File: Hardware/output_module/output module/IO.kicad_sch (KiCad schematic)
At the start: 30 parts, among them J2 thonkiconn, J3 thonkiconn, J4 Conn_01x03, J4 thonkiconn, U1 MAX97220C, U2 TL074

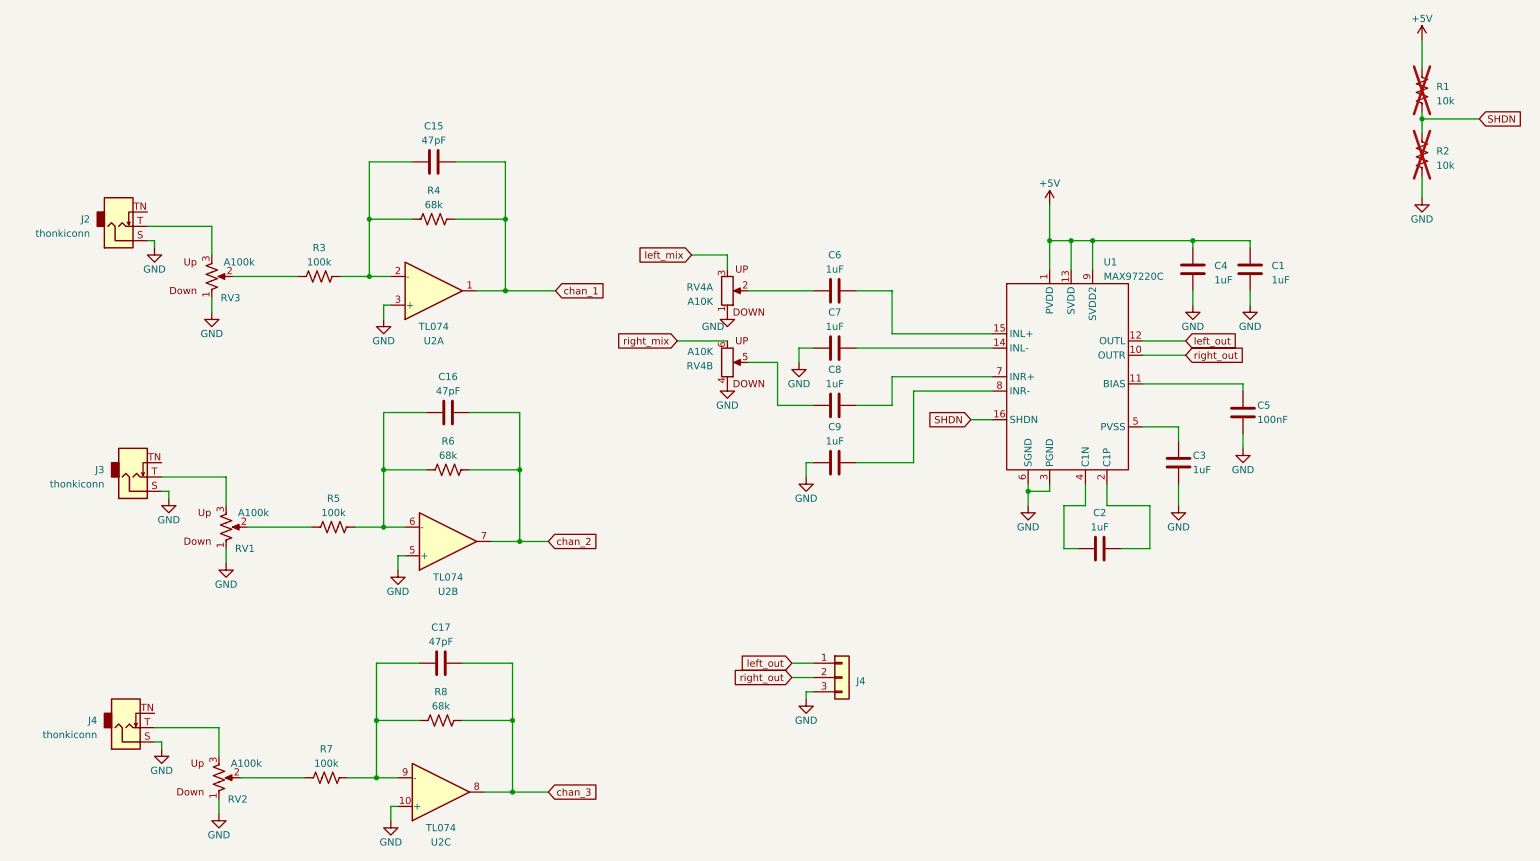
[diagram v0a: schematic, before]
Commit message: proto order
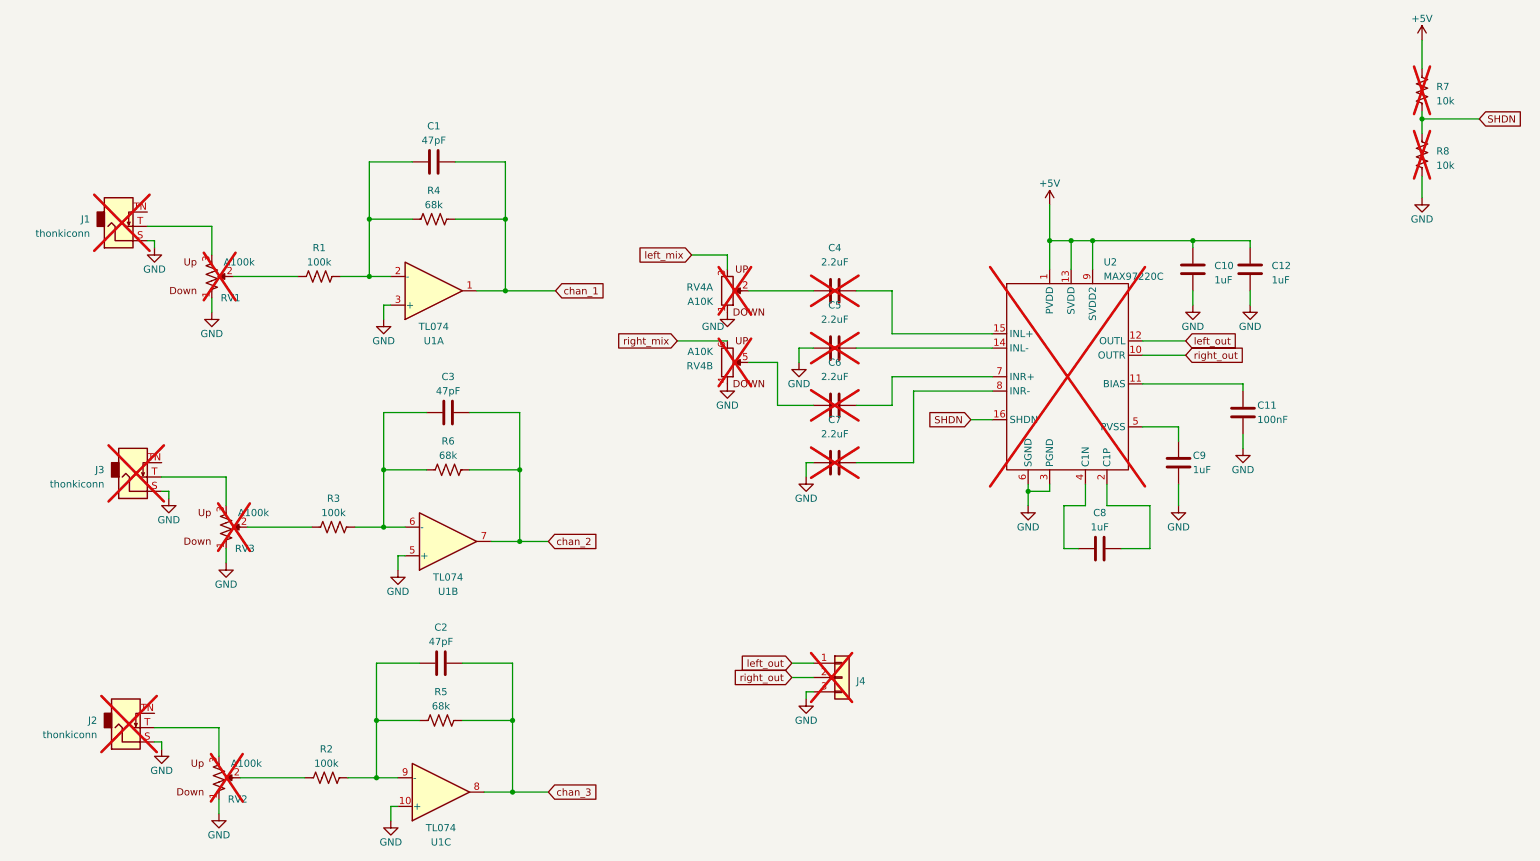
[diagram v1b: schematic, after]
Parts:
- removed C6, C7, C8, C9: 1uF, Capacitor_THT:C_Rect_L7.2mm_W4.5mm_P5.00mm_FKS2_FKP2_MKS2_MKP2, symbol synthesis:CAP_1UF_FILM
- added C4, C5, C6, C7: 2.2uF, Capacitor_THT:C_Rect_L7.2mm_W4.5mm_P5.00mm_FKS2_FKP2_MKS2_MKP2, symbol synthesis:CAP_2.2UF_FILM
- J1: renamed from J2; now not fitted
- J2: renamed from J4; now not fitted
- J3, J4, RV2, RV4: now not fitted
- RV1: renamed from RV3; now not fitted
- RV3: renamed from RV1; now not fitted
- U2: renamed from U1; now not fitted
- renumbered C15 to C1, C4 to C10, C5 to C11, C1 to C12, C17 to C2, C16 to C3, C2 to C8, C3 to C9, R3 to R1, R7 to R2, R5 to R3, R8 to R5, R1 to R7, R2 to R8, U2 to U1
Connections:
- net GND: now also C5.1, C7.1
- net at RV4.2: now also C4.1
- net at U2.8 (INR-): now also C7.2
- net at U2.14 (INL-): now also C5.2
- net at RV4.5: now also C6.1
- net at U2.7 (INR+): now also C6.2
- net at U2.15 (INL+): now also C4.2

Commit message: update output module production mistakes
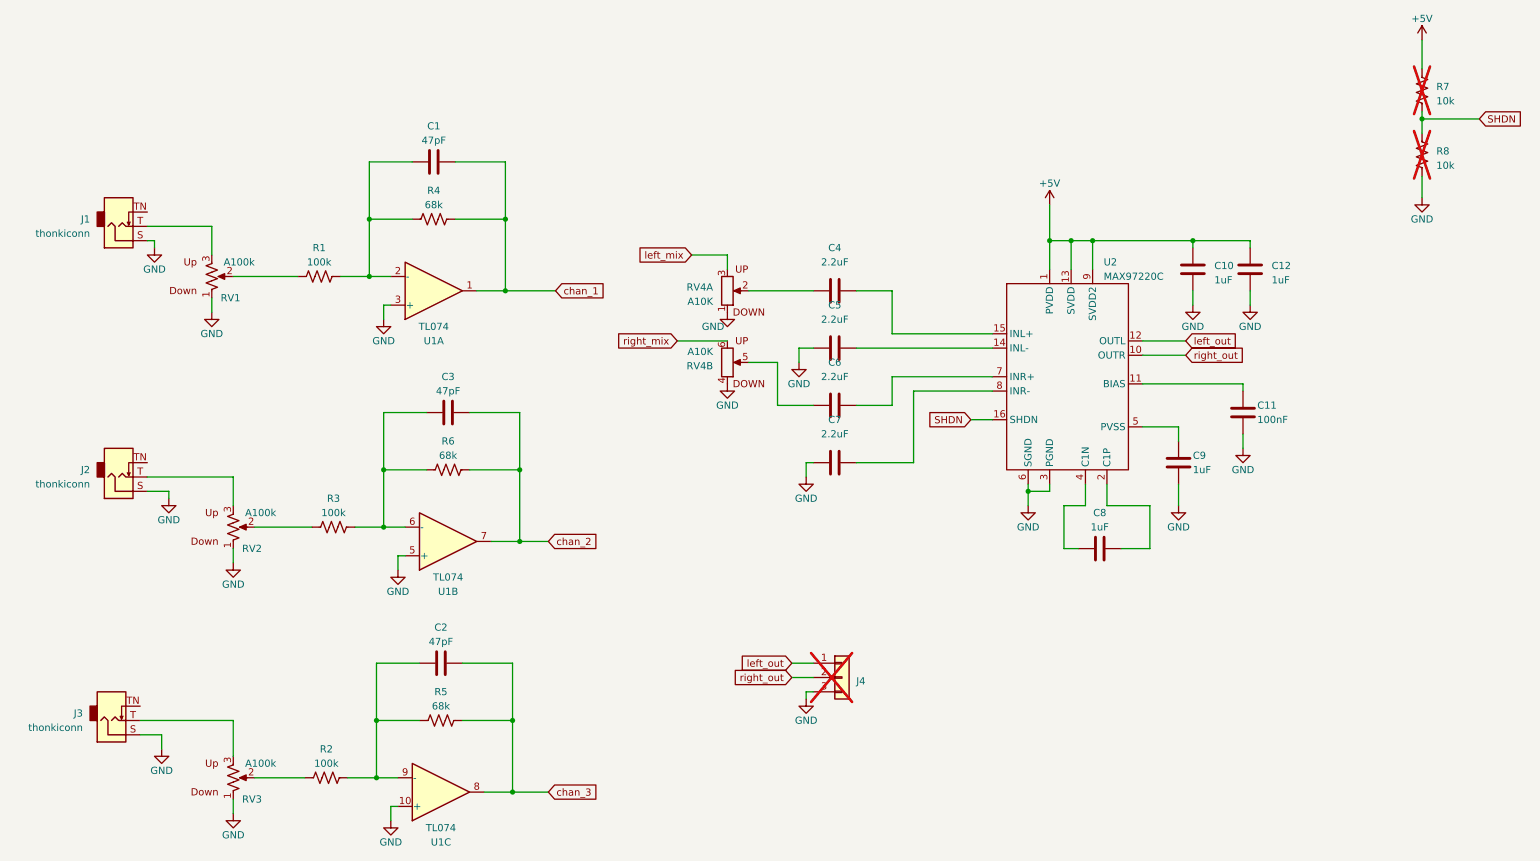
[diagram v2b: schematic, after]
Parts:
- C4, C5, C6, C7: footprint Capacitor_THT:C_Rect_L7.2mm_W4.5mm_P5.00mm_FKS2_FKP2_MKS2_MKP2 -> synthesis:C_Rect_L7.8mm_W7.8mm_P5.00mm; now fitted
- J1, J2, J3, RV1, RV2, RV3, RV4, U2: now fitted
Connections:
- net at RV3.2: now also R2.1; no longer R3.1
- net at RV2.2: now also R3.1; no longer R2.1
